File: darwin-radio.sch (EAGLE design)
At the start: 50 parts, among them J1 S1911-46R, Q2 NDS8434, U1 ATWINC, U2 INA219, U6 MCP7384X

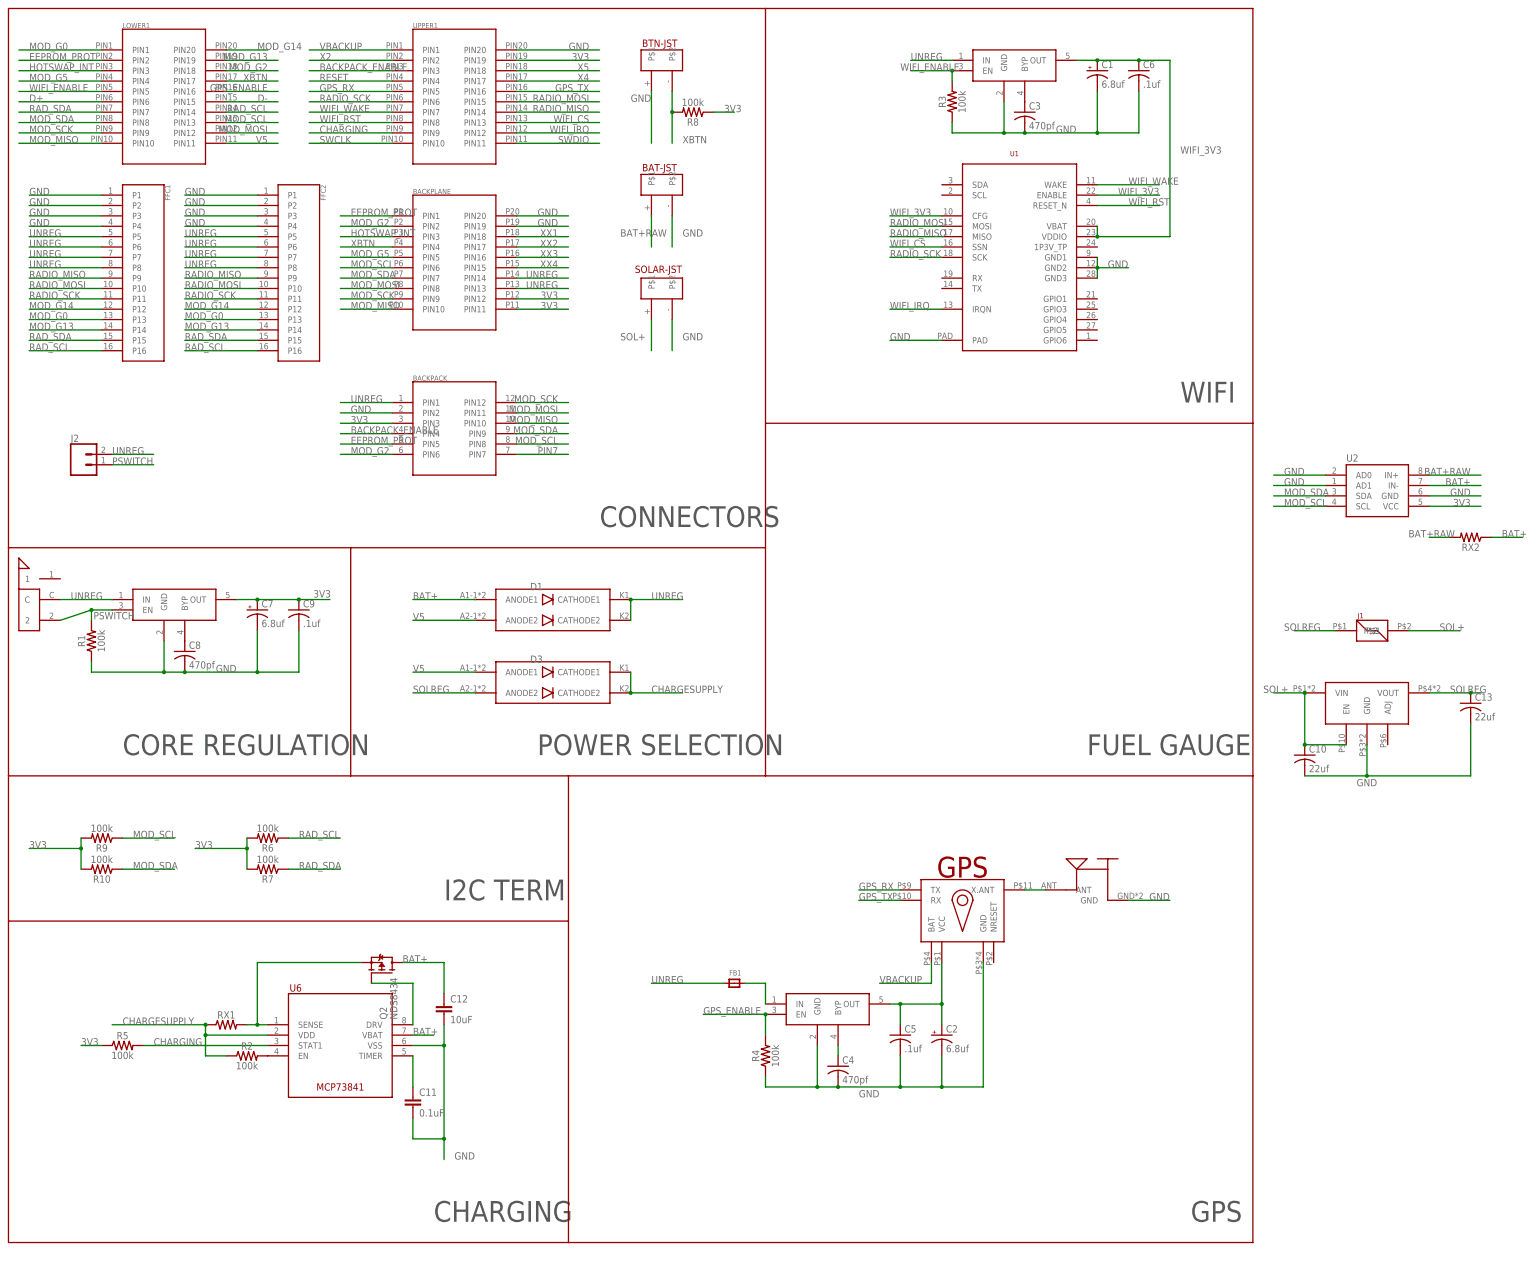
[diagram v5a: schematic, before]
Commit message: Toughened up connector footprints, cleaned up schematic, added schematic PDF.
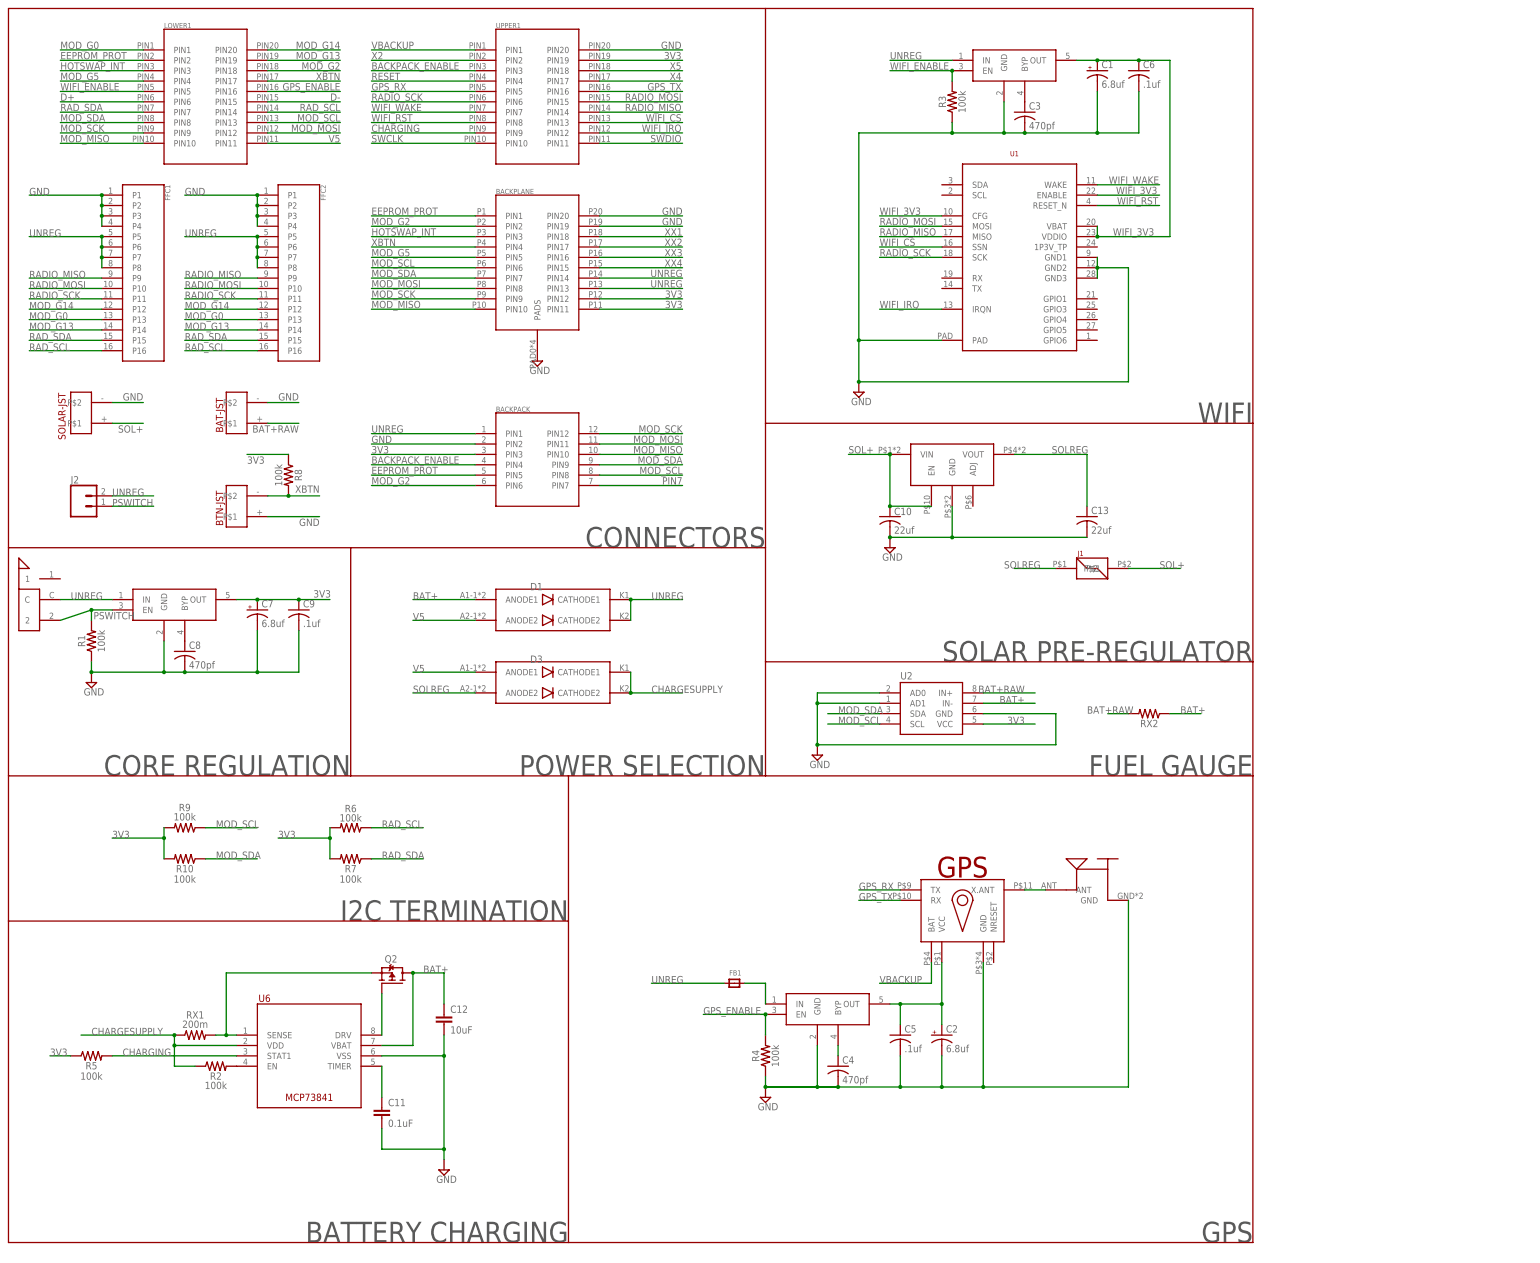
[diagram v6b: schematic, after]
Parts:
- RX1: value 100M -> 200m
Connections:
- net GND: now also BACKPLANE.PADS
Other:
- note added: "BATTERY CHARGING"
- note added: "I2C TERMINATION"
- note added: "SOLAR PRE-REGULATOR"
- note removed: "CHARGING"
- note removed: "I2C TERM"
- moved on the sheet: BACKPACK, BAT-JST, BTN-JST, C10, C11, C12, C13, J1, J2, LOWER1, Q2, R10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

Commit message: Transitioned from 4 to 2 layers. Added solar power monitor. Changed GPS to L80-M39.
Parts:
- removed FFC2: 505110-1692, Conservify:505110-1692
- added C14, C15: .1uf, rcl:C-USC0603K
- added RX3: 100M, rcl:R-US_R2512
- added U3: INA219, Conservify:INA219
- U$1: value FGPMMOPA6H -> FGPMMOPA6HL80; device Conservify:FGPMMOPA6H -> Conservify:FGPMMOPA6HL80
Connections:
- new net SOL+RAW: RX3.2, SOLAR-JST.P$1, U3.IN+
- net 3V3: now also C14.1, C15.1, U3.AD0, U3.VCC
- net GND: now also BAT-JST.PADS, BTN-JST.PADS, C14.2, C15.2, SOLAR-JST.PADS, U3.AD1, U3.GND; no longer FFC2.P1, FFC2.P2, FFC2.P3, FFC2.P4
- net MOD_G0: no longer FFC2.P13
- net MOD_G13: no longer FFC2.P14
- net MOD_G14: no longer FFC2.P12
- net MOD_SCL: now also U3.SCL
- net MOD_SDA: now also U3.SDA
- net RADIO_MISO: no longer FFC2.P9
- net RADIO_MOSI: no longer FFC2.P10
- net RADIO_SCK: no longer FFC2.P11
- net RAD_SCL: no longer FFC2.P16
- net RAD_SDA: no longer FFC2.P15
- net SOL+: now also RX3.1, U3.IN-; no longer SOLAR-JST.P$1
- net UNREG: now also U$1.BAT; no longer FFC2.P5, FFC2.P6, FFC2.P7, FFC2.P8
- net VBACKUP: no longer U$1.BAT
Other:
- note added: "POWER MONITORING"
- note removed: "FUEL GAUGE"
- moved on the sheet: C10, C13, J1
